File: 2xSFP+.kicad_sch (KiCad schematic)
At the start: 63 parts, among them J2 Bel-Fuse_SFP+_2x20_SS-79100-0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, U5 PCA9539AHF

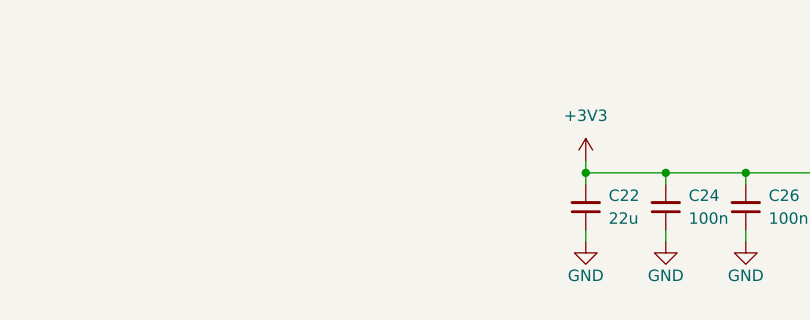
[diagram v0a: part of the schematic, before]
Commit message: [#70030] Unify functional block names
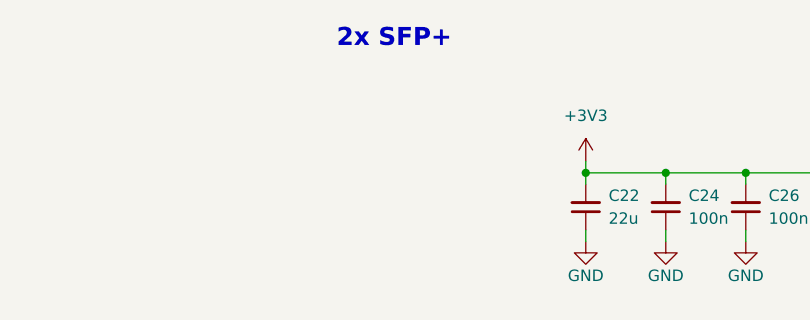
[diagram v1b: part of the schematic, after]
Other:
- note added: "2x SFP+"
- company: Antmicro Ltd. -> Antmicro Ltd
- title: Com Express 7 baseboard -> COM Express 7 Baseboard
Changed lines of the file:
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@@
 	(paper "A3")
 	(title_block
-		(title "Com Express 7 baseboard")
-		(date "2024-03-28")
+		(title "COM Express 7 Baseboard")
+		(date "2024-12-13")
 		(rev "1.1.0")
-		(company "Antmicro Ltd.")
+		(company "Antmicro Ltd")
+		(comment 1 "www.antmicro.com")
 	)
 	(junction
@@
 		)
 	)
+	(text "2x SFP+"
+		(exclude_from_sim no)
+		(at 204.724 21.844 0)
+		(effects
+			(font
+				(size 2 2)
+				(thickness 0.4)
+				(bold yes)
+			)
+			(justify left bottom)
+		)
+	)

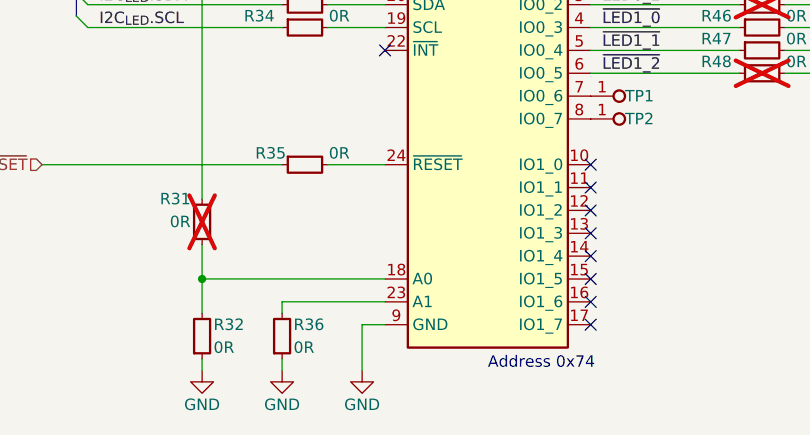
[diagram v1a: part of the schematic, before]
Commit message: [#70532] Change U5 I2C address to 0x75
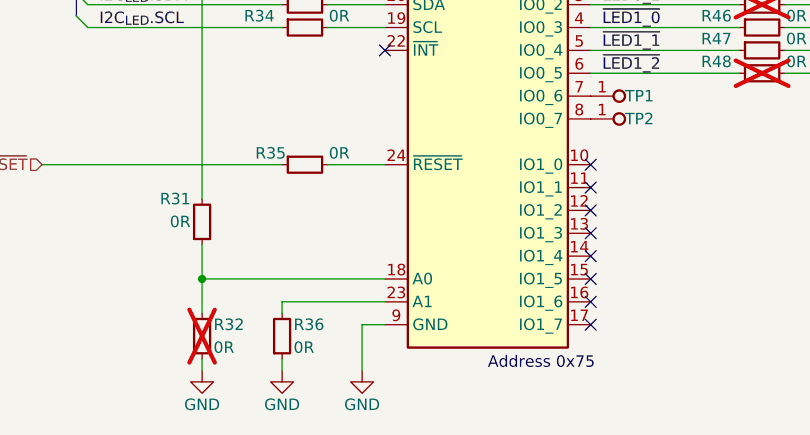
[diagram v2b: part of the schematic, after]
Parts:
- R31: now fitted
- R32: now not fitted
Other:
- note added: "Address 0x75"
- note removed: "Address 0x74"
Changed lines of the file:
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@@
 		)
 	)
-	(text "Address 0x74\n"
+	(text "Address 0x75"
 		(exclude_from_sim no)
 		(at 191.77 274.32 0)
@@
 		(in_bom yes)
 		(on_board yes)
-		(dnp no)
+		(dnp yes)
 		(property "Reference" "R32"
 			(at 161.29 269.24 90)
@@
 		(in_bom yes)
 		(on_board yes)
-		(dnp yes)
+		(dnp no)
 		(property "Reference" "R31"
 			(at 158.75 255.27 90)
